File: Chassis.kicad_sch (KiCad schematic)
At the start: 16 parts, among them J1 Conn_01x02, J10 Conn_01x02, J2 Conn_01x02, J3 Conn_01x02, J4 Conn_01x02, J5 Conn_01x02, J6 Conn_01x02, J7 Conn_01x02, J8 Conn_01x02, J9 Conn_01x02

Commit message: Finalized board design
I think
Also added more 3D models and whatnot
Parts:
- J10, J2, J4, J8: footprint Connector_AMASS:AMASS_XT30U-F_1x02_P5.0mm_Vertical -> Robomaster_ICs:AMASS_XT30U-F_1x02_P5.0mm_Vertical
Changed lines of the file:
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@@
       (effects (font (size 1.27 1.27)) (justify left))
     )
-    (property "Footprint" "Connector_AMASS:AMASS_XT30U-F_1x02_P5.0mm_Vertical" (at 128.27 97.79 0)
+    (property "Footprint" "Robomaster_ICs:AMASS_XT30U-F_1x02_P5.0mm_Vertical" (at 128.27 97.79 0)
       (effects (font (size 1.27 1.27)) hide)
     )
@@
       (effects (font (size 1.27 1.27)) (justify left))
     )
-    (property "Footprint" "Connector_AMASS:AMASS_XT30U-F_1x02_P5.0mm_Vertical" (at 128.27 123.19 0)
+    (property "Footprint" "Robomaster_ICs:AMASS_XT30U-F_1x02_P5.0mm_Vertical" (at 128.27 123.19 0)
       (effects (font (size 1.27 1.27)) hide)
     )
@@
       (effects (font (size 1.27 1.27)) (justify left))
     )
-    (property "Footprint" "Connector_AMASS:AMASS_XT30U-F_1x02_P5.0mm_Vertical" (at 128.27 148.59 0)
+    (property "Footprint" "Robomaster_ICs:AMASS_XT30U-F_1x02_P5.0mm_Vertical" (at 128.27 148.59 0)
       (effects (font (size 1.27 1.27)) hide)
     )
@@
       (effects (font (size 1.27 1.27)) (justify left))
     )
-    (property "Footprint" "Connector_AMASS:AMASS_XT30U-F_1x02_P5.0mm_Vertical" (at 128.27 72.39 0)
-      (effects (font (size 1.27 1.27)) hide)
-    )
+    (property "Footprint" "Robomaster_ICs:AMASS_XT30U-F_1x02_P5.0mm_Vertical" (at 128.27 72.39 0)
+      (effects (font (size 1.27 1.27)) hide)
+    )

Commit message: Add big boy connector
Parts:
- added J11: Sabre Vertical Header 6, Robomaster_ICs:CON_431602106_MOL, symbol Robomaster_Library:Sabre Vertical Header 6
- J1: value Conn_01x02 -> FR_JST
- J10: value Conn_01x02 -> BL_XT30
- J2: value Conn_01x02 -> FR_XT30
- J3: value Conn_01x02 -> BR_JST
- J4: value Conn_01x02 -> BR_XT30
- J5: value Conn_01x02 -> IN_JST
- J6: value Conn_01x02 -> IN_XT60
- J7: value Conn_01x02 -> FL_JST
- J8: value Conn_01x02 -> FL_XT30
- J9: value Conn_01x02 -> BL_JST
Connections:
- net GND: now also J11.B1, J11.B2, J11.D1, J11.D2, J11.F1, J11.F2
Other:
- note added: "Sabre Output Connector"
- moved on the sheet: J1, J10, J2, J3, J4, J7, J8, J9

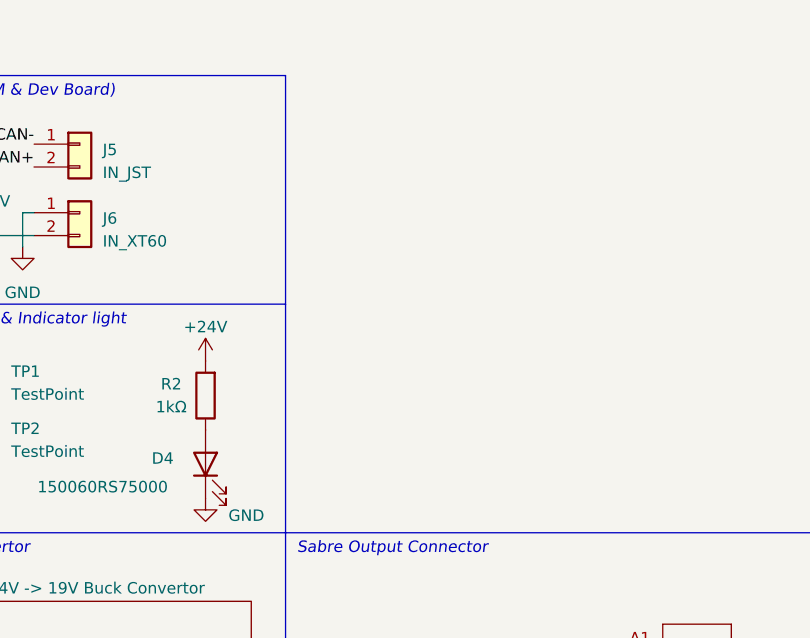
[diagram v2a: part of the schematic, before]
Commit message: Added mounting holes
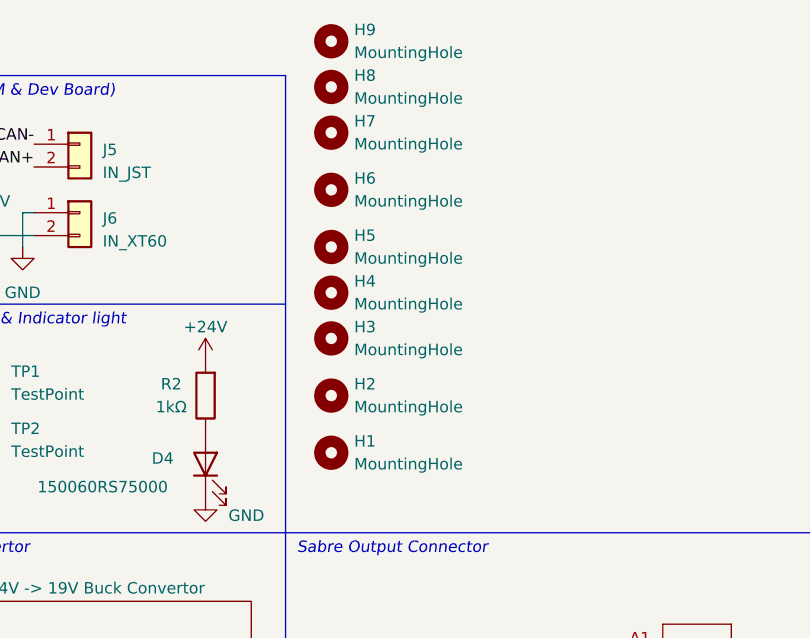
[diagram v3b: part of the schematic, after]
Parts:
- added H1, H2, H3, H4, H5, H6, H7, H8, H9: MountingHole, MountingHole:MountingHole_3.2mm_M3, symbol Mechanical:MountingHole
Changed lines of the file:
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@@
+    )
+  )
+  (symbol (lib_id "Mechanical:MountingHole") (at 196.85 99.06 0) (unit 1)
+    (in_bom yes) (on_board yes) (dnp no) (fields_autoplaced)
+    (property "Reference" "H1" (at 199.39 97.79 0)
+      (effects (font (size 1.27 1.27)) (justify left))
+    )
+    (property "Value" "MountingHole" (at 199.39 100.33 0)
+      (effects (font (size 1.27 1.27)) (justify left))
+    )
+    (property "Footprint" "MountingHole:MountingHole_3.2mm_M3" (at 196.85 99.06 0)
+      (effects (font (size 1.27 1.27)) hide)
+    )
+    (property "Datasheet" "~" (at 196.85 99.06 0)
+      (effects (font (size 1.27 1.27)) hide)
+    )
+    (instances
+      (project "Chassis"
+        (path "/d5f28ba3-2393-441a-9a3a-5aa9d797472a"
+          (reference "H1") (unit 1)
+        )
+      )
     )
   )
@@
     )
   )
+  (symbol (lib_id "Mechanical:MountingHole") (at 196.85 63.5 0) (unit 1)
+    (in_bom yes) (on_board yes) (dnp no) (fields_autoplaced)
+    (property "Reference" "H7" (at 199.39 62.23 0)
+      (effects (font (size 1.27 1.27)) (justify left))
+    )
+    (property "Value" "MountingHole" (at 199.39 64.77 0)
+      (effects (font (size 1.27 1.27)) (justify left))
+    )
+    (property "Footprint" "MountingHole:MountingHole_3.2mm_M3" (at 196.85 63.5 0)
+      (effects (font (size 1.27 1.27)) hide)
+    )
+    (property "Datasheet" "~" (at 196.85 63.5 0)
+      (effects (font (size 1.27 1.27)) hide)
+    )
+    (instances
+      (project "Chassis"
+        (path "/d5f28ba3-2393-441a-9a3a-5aa9d797472a"
+          (reference "H7") (unit 1)
+        )
+      )
+    )
+  )
   (symbol (lib_id "power:+24V") (at 140.97 149.86 0) (unit 1)
     (in_bom yes) (on_board yes) (dnp no) (fields_autoplaced)
@@
         (path "/d5f28ba3-2393-441a-9a3a-5aa9d797472a"
           (reference "#PWR010") (unit 1)
+        )
+      )
+    )
+  )
+  (symbol (lib_id "Mechanical:MountingHole") (at 196.85 92.71 0) (unit 1)
+    (in_bom yes) (on_board yes) (dnp no) (fields_autoplaced)
+    (property "Reference" "H2" (at 199.39 91.44 0)
+      (effects (font (size 1.27 1.27)) (justify left))
+    )
+    (property "Value" "MountingHole" (at 199.39 93.98 0)
+      (effects (font (size 1.27 1.27)) (justify left))
+    )
+    (property "Footprint" "MountingHole:MountingHole_3.2mm_M3" (at 196.85 92.71 0)
+      (effects (font (size 1.27 1.27)) hide)
+    )
+    (property "Datasheet" "~" (at 196.85 92.71 0)
+      (effects (font (size 1.27 1.27)) hide)
+    )
+    (instances
+      (project "Chassis"
+        (path "/d5f28ba3-2393-441a-9a3a-5aa9d797472a"
+          (reference "H2") (unit 1)
         )
       )
@@
     )
   )
+  (symbol (lib_id "Mechanical:MountingHole") (at 196.85 76.2 0) (unit 1)
+    (in_bom yes) (on_board yes) (dnp no) (fields_autoplaced)
+    (property "Reference" "H5" (at 199.39 74.93 0)
+      (effects (font (size 1.27 1.27)) (justify left))
+    )
+    (property "Value" "MountingHole" (at 199.39 77.47 0)
+      (effects (font (size 1.27 1.27)) (justify left))
+    )
+    (property "Footprint" "MountingHole:MountingHole_3.2mm_M3" (at 196.85 76.2 0)
+      (effects (font (size 1.27 1.27)) hide)
+    )
+    (property "Datasheet" "~" (at 196.85 76.2 0)
+      (effects (font (size 1.27 1.27)) hide)
+    )
+    (instances
+      (project "Chassis"
+        (path "/d5f28ba3-2393-441a-9a3a-5aa9d797472a"
+          (reference "H5") (unit 1)
+        )
+      )
+    )
+  )
   (symbol (lib_id "power:+24V") (at 154.94 120.65 0) (unit 1)
     (in_bom yes) (on_board yes) (dnp no) (fields_autoplaced)
@@
     )
   )
+  (symbol (lib_id "Mechanical:MountingHole") (at 196.85 53.34 0) (unit 1)
+    (in_bom yes) (on_board yes) (dnp no) (fields_autoplaced)
+    (property "Reference" "H9" (at 199.39 52.07 0)
+      (effects (font (size 1.27 1.27)) (justify left))
+    )
+    (property "Value" "MountingHole" (at 199.39 54.61 0)
+      (effects (font (size 1.27 1.27)) (justify left))
+    )
+    (property "Footprint" "MountingHole:MountingHole_3.2mm_M3" (at 196.85 53.34 0)
+      (effects (font (size 1.27 1.27)) hide)
+    )
+    (property "Datasheet" "~" (at 196.85 53.34 0)
+      (effects (font (size 1.27 1.27)) hide)
+    )
+    (instances
+      (project "Chassis"
+        (path "/d5f28ba3-2393-441a-9a3a-5aa9d797472a"
+          (reference "H9") (unit 1)
+        )
+      )
+    )
+  )
   (symbol (lib_id "Connector:TestPoint") (at 158.75 100.33 0) (unit 1)
     (in_bom yes) (on_board yes) (dnp no) (fields_autoplaced)
@@
         (path "/d5f28ba3-2393-441a-9a3a-5aa9d797472a"
           (reference "#PWR09") (unit 1)
+        )
+      )
+    )
+  )
+  (symbol (lib_id "Mechanical:MountingHole") (at 196.85 86.36 0) (unit 1)
+    (in_bom yes) (on_board yes) (dnp no) (fields_autoplaced)
+    (property "Reference" "H3" (at 199.39 85.09 0)
+      (effects (font (size 1.27 1.27)) (justify left))
+    )
+    (property "Value" "MountingHole" (at 199.39 87.63 0)
+      (effects (font (size 1.27 1.27)) (justify left))
+    )
+    (property "Footprint" "MountingHole:MountingHole_3.2mm_M3" (at 196.85 86.36 0)
+      (effects (font (size 1.27 1.27)) hide)
+    )
+    (property "Datasheet" "~" (at 196.85 86.36 0)
+      (effects (font (size 1.27 1.27)) hide)
+    )
+    (instances
+      (project "Chassis"
+        (path "/d5f28ba3-2393-441a-9a3a-5aa9d797472a"
+          (reference "H3") (unit 1)
+        )
+      )
+    )
+  )
+  (symbol (lib_id "Mechanical:MountingHole") (at 196.85 81.28 0) (unit 1)
+    (in_bom yes) (on_board yes) (dnp no) (fields_autoplaced)
+    (property "Reference" "H4" (at 199.39 80.01 0)
+      (effects (font (size 1.27 1.27)) (justify left))
+    )
+    (property "Value" "MountingHole" (at 199.39 82.55 0)
+      (effects (font (size 1.27 1.27)) (justify left))
+    )
+    (property "Footprint" "MountingHole:MountingHole_3.2mm_M3" (at 196.85 81.28 0)
+      (effects (font (size 1.27 1.27)) hide)
+    )
+    (property "Datasheet" "~" (at 196.85 81.28 0)
+      (effects (font (size 1.27 1.27)) hide)
+    )
+    (instances
+      (project "Chassis"
+        (path "/d5f28ba3-2393-441a-9a3a-5aa9d797472a"
+          (reference "H4") (unit 1)
         )
       )
@@
     )
   )
+  (symbol (lib_id "Mechanical:MountingHole") (at 196.85 58.42 0) (unit 1)
+    (in_bom yes) (on_board yes) (dnp no) (fields_autoplaced)
+    (property "Reference" "H8" (at 199.39 57.15 0)
+      (effects (font (size 1.27 1.27)) (justify left))
+    )
+    (property "Value" "MountingHole" (at 199.39 59.69 0)
+      (effects (font (size 1.27 1.27)) (justify left))
+    )
+    (property "Footprint" "MountingHole:MountingHole_3.2mm_M3" (at 196.85 58.42 0)
+      (effects (font (size 1.27 1.27)) hide)
+    )
+    (property "Datasheet" "~" (at 196.85 58.42 0)
+      (effects (font (size 1.27 1.27)) hide)
+    )
+    (instances
+      (project "Chassis"
+        (path "/d5f28ba3-2393-441a-9a3a-5aa9d797472a"
+          (reference "H8") (unit 1)
+        )
+      )
+    )
+  )
   (symbol (lib_id "Connector_Generic:Conn_01x02") (at 130.81 147.32 0) (mirror y) (unit 1)
     (in_bom yes) (on_board yes) (dnp no) (fields_autoplaced)
@@
         )
       )
+    )
+  )
+  (symbol (lib_id "Mechanical:MountingHole") (at 196.85 69.85 0) (unit 1)
+    (in_bom yes) (on_board yes) (dnp no) (fields_autoplaced)
+    (property "Reference" "H6" (at 199.39 68.58 0)
+      (effects (font (size 1.27 1.27)) (justify left))
+    )
+    (property "Value" "MountingHole" (at 199.39 71.12 0)
+      (effects (font (size 1.27 1.27)) (justify left))
+    )
+    (property "Footprint" "MountingHole:MountingHole_3.2mm_M3" (at 196.85 69.85 0)
+      (effects (font (size 1.27 1.27)) hide)
+    )
+    (property "Datasheet" "~" (at 196.85 69.85 0)
+      (effects (font (size 1.27 1.27)) hide)
+    )
+    (instances
+      (project "Chassis"
+        (path "/d5f28ba3-2393-441a-9a3a-5aa9d797472a"
+          (reference "H6") (unit 1)
+        )
+      )

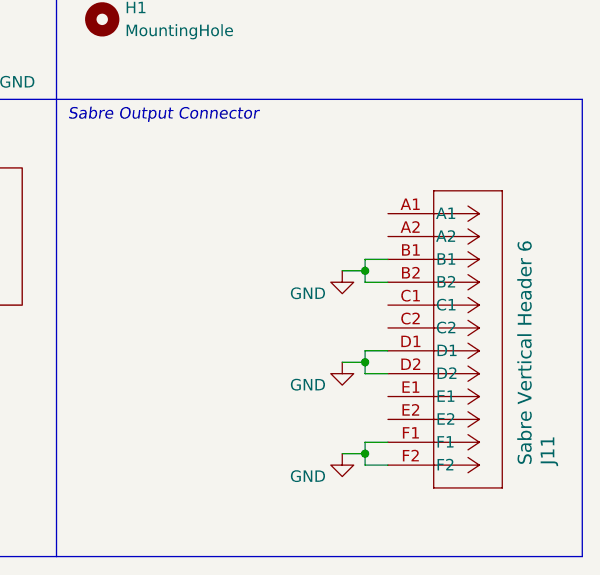
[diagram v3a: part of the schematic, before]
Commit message: Added pour for output
Will need to add +5V buck + data connector + new power connector

AAAAAAAAAAAAAAAAAAAAAAA
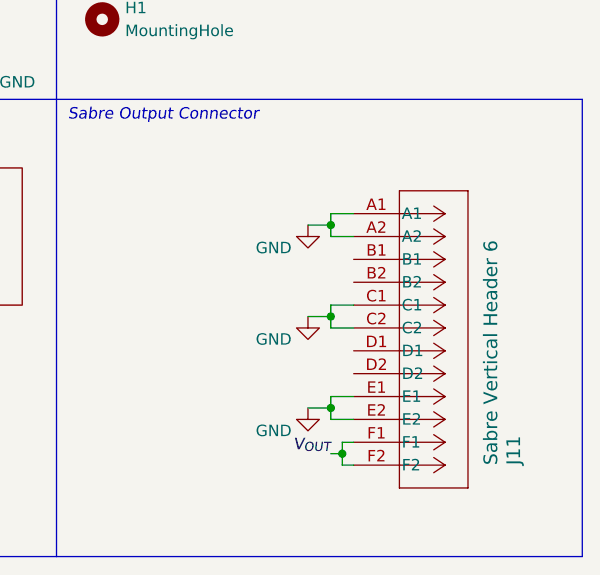
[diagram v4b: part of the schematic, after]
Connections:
- net GND: now also J11.A1, J11.A2, J11.C1, J11.C2, J11.E1, J11.E2; no longer J11.B1, J11.B2, J11.D1, J11.D2, J11.F1, J11.F2
- net V_{OUT}: now also J11.F1, J11.F2
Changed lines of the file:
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@@
 (kicad_sch (version 20230121) (generator eeschema)
   (paper "A4")
-  (junction (at 226.06 127) (diameter 0) (color 0 0 0 0)
-  )
-  (junction (at 226.06 137.16) (diameter 0) (color 0 0 0 0)
-  )
-  (junction (at 226.06 147.32) (diameter 0) (color 0 0 0 0)
+  (junction (at 223.52 147.32) (diameter 0) (color 0 0 0 0)
+  )
+  (junction (at 222.25 121.92) (diameter 0) (color 0 0 0 0)
+  )
+  (junction (at 222.25 132.08) (diameter 0) (color 0 0 0 0)
+  )
+  (junction (at 222.25 142.24) (diameter 0) (color 0 0 0 0)
   )
   (polyline (pts (xy 191.77 82.55) (xy 191.77 107.95))
     (stroke (width 0) (type default))
   )
+  (wire (pts (xy 222.25 147.32) (xy 223.52 147.32))
+    (stroke (width 0) (type default))
+  )
   (wire (pts (xy 167.64 144.78) (xy 168.91 144.78))
     (stroke (width 0) (type default))
@@
     (stroke (width 0) (type default))
   )
+  (wire (pts (xy 223.52 146.05) (xy 223.52 147.32))
+    (stroke (width 0) (type default))
+  )
   (wire (pts (xy 157.48 127) (xy 158.75 127))
     (stroke (width 0) (type default))
   )
-  (wire (pts (xy 228.6 146.05) (xy 226.06 146.05))
+  (wire (pts (xy 224.79 140.97) (xy 222.25 140.97))
+    (stroke (width 0) (type default))
+  )
+  (wire (pts (xy 224.79 146.05) (xy 223.52 146.05))
     (stroke (width 0) (type default))
   )
@@
     (stroke (width 0) (type default))
   )
-  (wire (pts (xy 228.6 138.43) (xy 226.06 138.43))
+  (wire (pts (xy 224.79 133.35) (xy 222.25 133.35))
     (stroke (width 0) (type default))
   )
@@
     (stroke (width 0) (type default))
   )
-  (wire (pts (xy 228.6 148.59) (xy 226.06 148.59))
+  (wire (pts (xy 224.79 143.51) (xy 222.25 143.51))
     (stroke (width 0) (type default))
   )
@@
     (stroke (width 0) (type default))
   )
-  (wire (pts (xy 226.06 147.32) (xy 223.52 147.32))
+  (wire (pts (xy 222.25 142.24) (xy 219.71 142.24))
     (stroke (width 0) (type default))
   )
@@
     (stroke (width 0) (type default))
   )
-  (wire (pts (xy 226.06 146.05) (xy 226.06 147.32))
+  (wire (pts (xy 222.25 140.97) (xy 222.25 142.24))
     (stroke (width 0) (type default))
   )
@@
     (stroke (width 0) (type default))
   )
-  (wire (pts (xy 226.06 135.89) (xy 226.06 137.16))
+  (wire (pts (xy 222.25 130.81) (xy 222.25 132.08))
     (stroke (width 0) (type default))
   )
@@
     (stroke (width 0) (type default))
   )
-  (wire (pts (xy 226.06 148.59) (xy 226.06 147.32))
+  (wire (pts (xy 222.25 143.51) (xy 222.25 142.24))
     (stroke (width 0) (type default))
   )
@@
     (stroke (width 0) (type default))
   )
-  (wire (pts (xy 226.06 138.43) (xy 226.06 137.16))
+  (wire (pts (xy 222.25 133.35) (xy 222.25 132.08))
     (stroke (width 0) (type default))
   )
@@
     (stroke (width 0) (type default))
   )
-  (wire (pts (xy 226.06 125.73) (xy 226.06 127))
-    (stroke (width 0) (type default))
-  )
-  (wire (pts (xy 228.6 128.27) (xy 226.06 128.27))
-    (stroke (width 0) (type default))
-  )
-  (wire (pts (xy 226.06 137.16) (xy 223.52 137.16))
+  (wire (pts (xy 222.25 120.65) (xy 222.25 121.92))
+    (stroke (width 0) (type default))
+  )
+  (wire (pts (xy 224.79 123.19) (xy 222.25 123.19))
+    (stroke (width 0) (type default))
+  )
+  (wire (pts (xy 222.25 132.08) (xy 219.71 132.08))
     (stroke (width 0) (type default))
   )
@@
     (stroke (width 0) (type default))
   )
+  (wire (pts (xy 223.52 147.32) (xy 223.52 148.59))
+    (stroke (width 0) (type default))
+  )
   (wire (pts (xy 137.16 121.92) (xy 135.89 121.92))
     (stroke (width 0) (type default))
   )
-  (wire (pts (xy 226.06 127) (xy 223.52 127))
+  (wire (pts (xy 222.25 121.92) (xy 219.71 121.92))
     (stroke (width 0) (type default))
   )
@@
     (stroke (width 0) (type default))
   )
-  (wire (pts (xy 228.6 125.73) (xy 226.06 125.73))
+  (wire (pts (xy 224.79 120.65) (xy 222.25 120.65))
     (stroke (width 0) (type default))
   )
@@
     (stroke (width 0) (type default))
   )
-  (wire (pts (xy 226.06 128.27) (xy 226.06 127))
-    (stroke (width 0) (type default))
-  )
-  (wire (pts (xy 228.6 135.89) (xy 226.06 135.89))
+  (wire (pts (xy 223.52 148.59) (xy 224.79 148.59))
+    (stroke (width 0) (type default))
+  )
+  (wire (pts (xy 222.25 123.19) (xy 222.25 121.92))
+    (stroke (width 0) (type default))
+  )
+  (wire (pts (xy 224.79 130.81) (xy 222.25 130.81))
     (stroke (width 0) (type default))
   )
@@
     (effects (font (size 1.27 1.27)) (justify left bottom))
   )
+  (label "V_{OUT}" (at 222.25 147.32 180) (fields_autoplaced)
+    (effects (font (size 1.27 1.27) italic) (justify right bottom))
+  )
   (label "CAN+" (at 163.83 67.31 180) (fields_autoplaced)
     (effects (font (size 1.27 1.27)) (justify right bottom))
@@
     )
   )
-  (symbol (lib_id "power:GND") (at 223.52 137.16 0) (unit 1)
+  (symbol (lib_id "power:GND") (at 219.71 132.08 0) (unit 1)
     (in_bom yes) (on_board yes) (dnp no)
-    (property "Reference" "#PWR028" (at 223.52 143.51 0)
-      (effects (font (size 1.27 1.27)) hide)
-    )
-    (property "Value" "GND" (at 219.71 139.7 0)
-      (effects (font (size 1.27 1.27)))
-    )
-    (property "Footprint" "" (at 223.52 137.16 0)
-      (effects (font (size 1.27 1.27)) hide)
-    )
-    (property "Datasheet" "" (at 223.52 137.16 0)
+    (property "Reference" "#PWR028" (at 219.71 138.43 0)
+      (effects (font (size 1.27 1.27)) hide)
+    )
+    (property "Value" "GND" (at 215.9 134.62 0)
+      (effects (font (size 1.27 1.27)))
+    )
+    (property "Footprint" "" (at 219.71 132.08 0)
+      (effects (font (size 1.27 1.27)) hide)
+    )
+    (property "Datasheet" "" (at 219.71 132.08 0)
       (effects (font (size 1.27 1.27)) hide)
     )
@@
     )
   )
-  (symbol (lib_id "Robomaster_Library:Sabre Vertical Header 6") (at 228.6 120.65 0) (unit 1)
+  (symbol (lib_id "Robomaster_Library:Sabre Vertical Header 6") (at 224.79 120.65 0) (unit 1)
     (in_bom yes) (on_board yes) (dnp no)
-    (property "Reference" "J11" (at 246.38 148.59 90)
+    (property "Reference" "J11" (at 242.57 148.59 90)
       (effects (font (size 1.524 1.524)) (justify left))
     )
-    (property "Value" "Sabre Vertical Header 6" (at 243.84 148.59 90)
+    (property "Value" "Sabre Vertical Header 6" (at 240.03 148.59 90)
       (effects (font (size 1.524 1.524)) (justify left))
     )
-    (property "Footprint" "Robomaster_ICs:CON_431602106_MOL" (at 228.6 120.65 0)
+    (property "Footprint" "Robomaster_ICs:CON_431602106_MOL" (at 224.79 120.65 0)
       (effects (font (size 1.27 1.27) italic) hide)
     )
-    (property "Datasheet" "https://www.molex.com/en-us/products/part-detail/431602106?display=pdf" (at 228.6 120.65 0)
+    (property "Datasheet" "https://www.molex.com/en-us/products/part-detail/431602106?display=pdf" (at 224.79 120.65 0)
       (effects (font (size 1.27 1.27) italic) hide)
     )
@@
     )
   )
-  (symbol (lib_id "power:GND") (at 223.52 127 0) (unit 1)
+  (symbol (lib_id "power:GND") (at 219.71 121.92 0) (unit 1)
     (in_bom yes) (on_board yes) (dnp no)
-    (property "Reference" "#PWR027" (at 223.52 133.35 0)
-      (effects (font (size 1.27 1.27)) hide)
-    )
-    (property "Value" "GND" (at 219.71 129.54 0)
-      (effects (font (size 1.27 1.27)))
-    )
-    (property "Footprint" "" (at 223.52 127 0)
-      (effects (font (size 1.27 1.27)) hide)
-    )
-    (property "Datasheet" "" (at 223.52 127 0)
+    (property "Reference" "#PWR027" (at 219.71 128.27 0)
+      (effects (font (size 1.27 1.27)) hide)
+    )
+    (property "Value" "GND" (at 215.9 124.46 0)
+      (effects (font (size 1.27 1.27)))
+    )
+    (property "Footprint" "" (at 219.71 121.92 0)
+      (effects (font (size 1.27 1.27)) hide)
+    )
+    (property "Datasheet" "" (at 219.71 121.92 0)
       (effects (font (size 1.27 1.27)) hide)
     )
@@
     )
   )
-  (symbol (lib_id "power:GND") (at 223.52 147.32 0) (unit 1)
+  (symbol (lib_id "power:GND") (at 219.71 142.24 0) (unit 1)
     (in_bom yes) (on_board yes) (dnp no)
-    (property "Reference" "#PWR029" (at 223.52 153.67 0)
-      (effects (font (size 1.27 1.27)) hide)
-    )
-    (property "Value" "GND" (at 219.71 149.86 0)
-      (effects (font (size 1.27 1.27)))
-    )
-    (property "Footprint" "" (at 223.52 147.32 0)
-      (effects (font (size 1.27 1.27)) hide)
-    )
-    (property "Datasheet" "" (at 223.52 147.32 0)
-      (effects (font (size 1.27 1.27)) hide)
-    )
+    (property "Reference" "#PWR029" (at 219.71 148.59 0)
+      (effects (font (size 1.27 1.27)) hide)
+    )
+    (property "Value" "GND" (at 215.9 144.78 0)
+      (effects (font (size 1.27 1.27)))
+    )
+    (property "Footprint" "" (at 219.71 142.24 0)
+      (effects (font (size 1.27 1.27)) hide)
+    )
+    (property "Datasheet" "" (at 219.71 142.24 0)
+      (effects (font (size 1.27 1.27)) hide)
+    )
